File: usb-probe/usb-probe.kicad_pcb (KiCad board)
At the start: 2 copper layers, 36.6 x 26.7 mm, 5 parts, among them J1 USB_C_Plug, J2 Conn_02x09_Top_Bottom, J3 USB_C_Receptacle

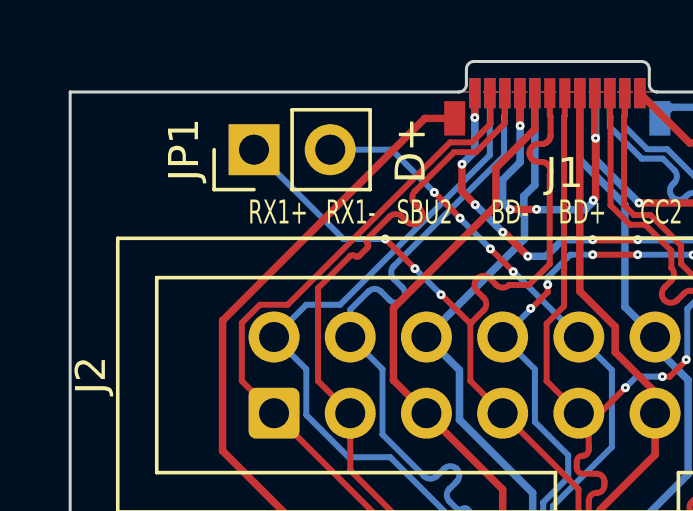
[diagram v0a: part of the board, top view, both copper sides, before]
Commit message: Attempt to equalise JP1 and JP2 D+/D- length
D+ and D- is a differential pair, so the tracks created by shorting JP1 and JP2
should be of equal length. I used the Python console to determine the track
lengths:

    import pcbnew
    sum(t.GetLength() for t in pcbnew.GetBoard().GetTracks() if t.IsSelected())

Which gave me a difference of about 7.2mm. I added another 4*1.6mm due to a
difference in via count.
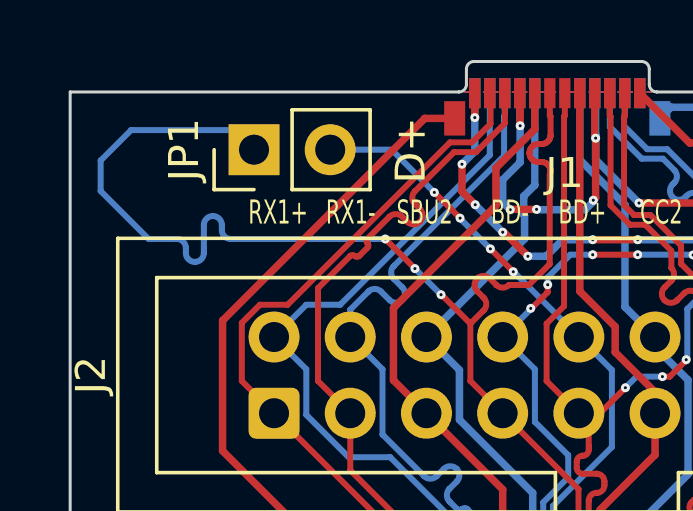
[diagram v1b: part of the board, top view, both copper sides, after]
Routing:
- net /A-D+: track 33.4 -> 47.0 mm
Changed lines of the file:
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@@
   (arc (start 144.994571 56.685149) (mid 144.782438 56.773017) (end 144.570305 56.685149) (width 0.2) (layer "F.Cu") (net 6))
   (arc (start 143.931044 56.470151) (mid 143.843176 56.682283) (end 143.931044 56.894415) (width 0.2) (layer "F.Cu") (net 6))
-  (segment (start 139.467902 55.151902) (end 136.492 52.176) (width 0.2) (layer "B.Cu") (net 6))
-  (segment (start 140.868556 55.151902) (end 139.467902 55.151902) (width 0.2) (layer "B.Cu") (net 6))
+  (segment (start 135.72 55.151902) (end 140.56831 55.151902) (width 0.2) (layer "B.Cu") (net 6))
+  (segment (start 134.22 55.451902) (end 134.22 55.61611) (width 0.2) (layer "B.Cu") (net 6))
+  (segment (start 131.38 52.538) (end 131.38 53.554) (width 0.2) (layer "B.Cu") (net 6))
+  (segment (start 136.492 52.176) (end 135.838 51.522) (width 0.2) (layer "B.Cu") (net 6))
+  (segment (start 132.396 51.522) (end 131.38 52.538) (width 0.2) (layer "B.Cu") (net 6))
+  (segment (start 131.38 53.554) (end 132.977902 55.151902) (width 0.2) (layer "B.Cu") (net 6))
   (segment (start 142.72579 57.009137) (end 141.855946 56.139293) (width 0.2) (layer "B.Cu") (net 6))
+  (segment (start 135.838 51.522) (end 132.396 51.522) (width 0.2) (layer "B.Cu") (net 6))
+  (segment (start 135.42 54.687719) (end 135.42 54.851902) (width 0.2) (layer "B.Cu") (net 6))
+  (segment (start 134.82 55.61611) (end 134.82 55.451902) (width 0.2) (layer "B.Cu") (net 6))
+  (segment (start 134.82 55.451902) (end 134.82 54.687719) (width 0.2) (layer "B.Cu") (net 6))
+  (segment (start 132.977902 55.151902) (end 133.92 55.151902) (width 0.2) (layer "B.Cu") (net 6))
+  (segment (start 140.56831 55.151902) (end 140.868556 55.151902) (width 0.2) (layer "B.Cu") (net 6))
+  (arc (start 133.92 55.151902) (mid 134.132132 55.23977) (end 134.22 55.451902) (width 0.2) (layer "B.Cu") (net 6))
+  (arc (start 134.82 54.687719) (mid 134.907868 54.475587) (end 135.12 54.387719) (width 0.2) (layer "B.Cu") (net 6))
+  (arc (start 135.12 54.387719) (mid 135.332132 54.475587) (end 135.42 54.687719) (width 0.2) (layer "B.Cu") (net 6))
+  (arc (start 135.42 54.851902) (mid 135.507868 55.064034) (end 135.72 55.151902) (width 0.2) (layer "B.Cu") (net 6))
+  (arc (start 134.52 55.91611) (mid 134.732132 55.828242) (end 134.82 55.61611) (width 0.2) (layer "B.Cu") (net 6))
+  (arc (start 134.22 55.61611) (mid 134.307868 55.828242) (end 134.52 55.91611) (width 0.2) (layer "B.Cu") (net 6))
   (segment (start 147.649546 61.289546) (end 147.32 60.96) (width 0.2) (layer "F.Cu") (net 7))
   (segment (start 150.352528 59.740117) (end 150.899119 59.193526) (width 0.2) (layer "F.Cu") (net 7))
